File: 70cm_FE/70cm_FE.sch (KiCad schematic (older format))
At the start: 150 parts, among them J2 U.FL, J3 U.FL, J4 U.FL, Q1 2SC3356, Q2 2SC3356, Q3 2SC3356, Q4 2N7002, U1 HT7533-1, U2 74HC14, U3 74HC14, U4 LM393, U5 M68710L

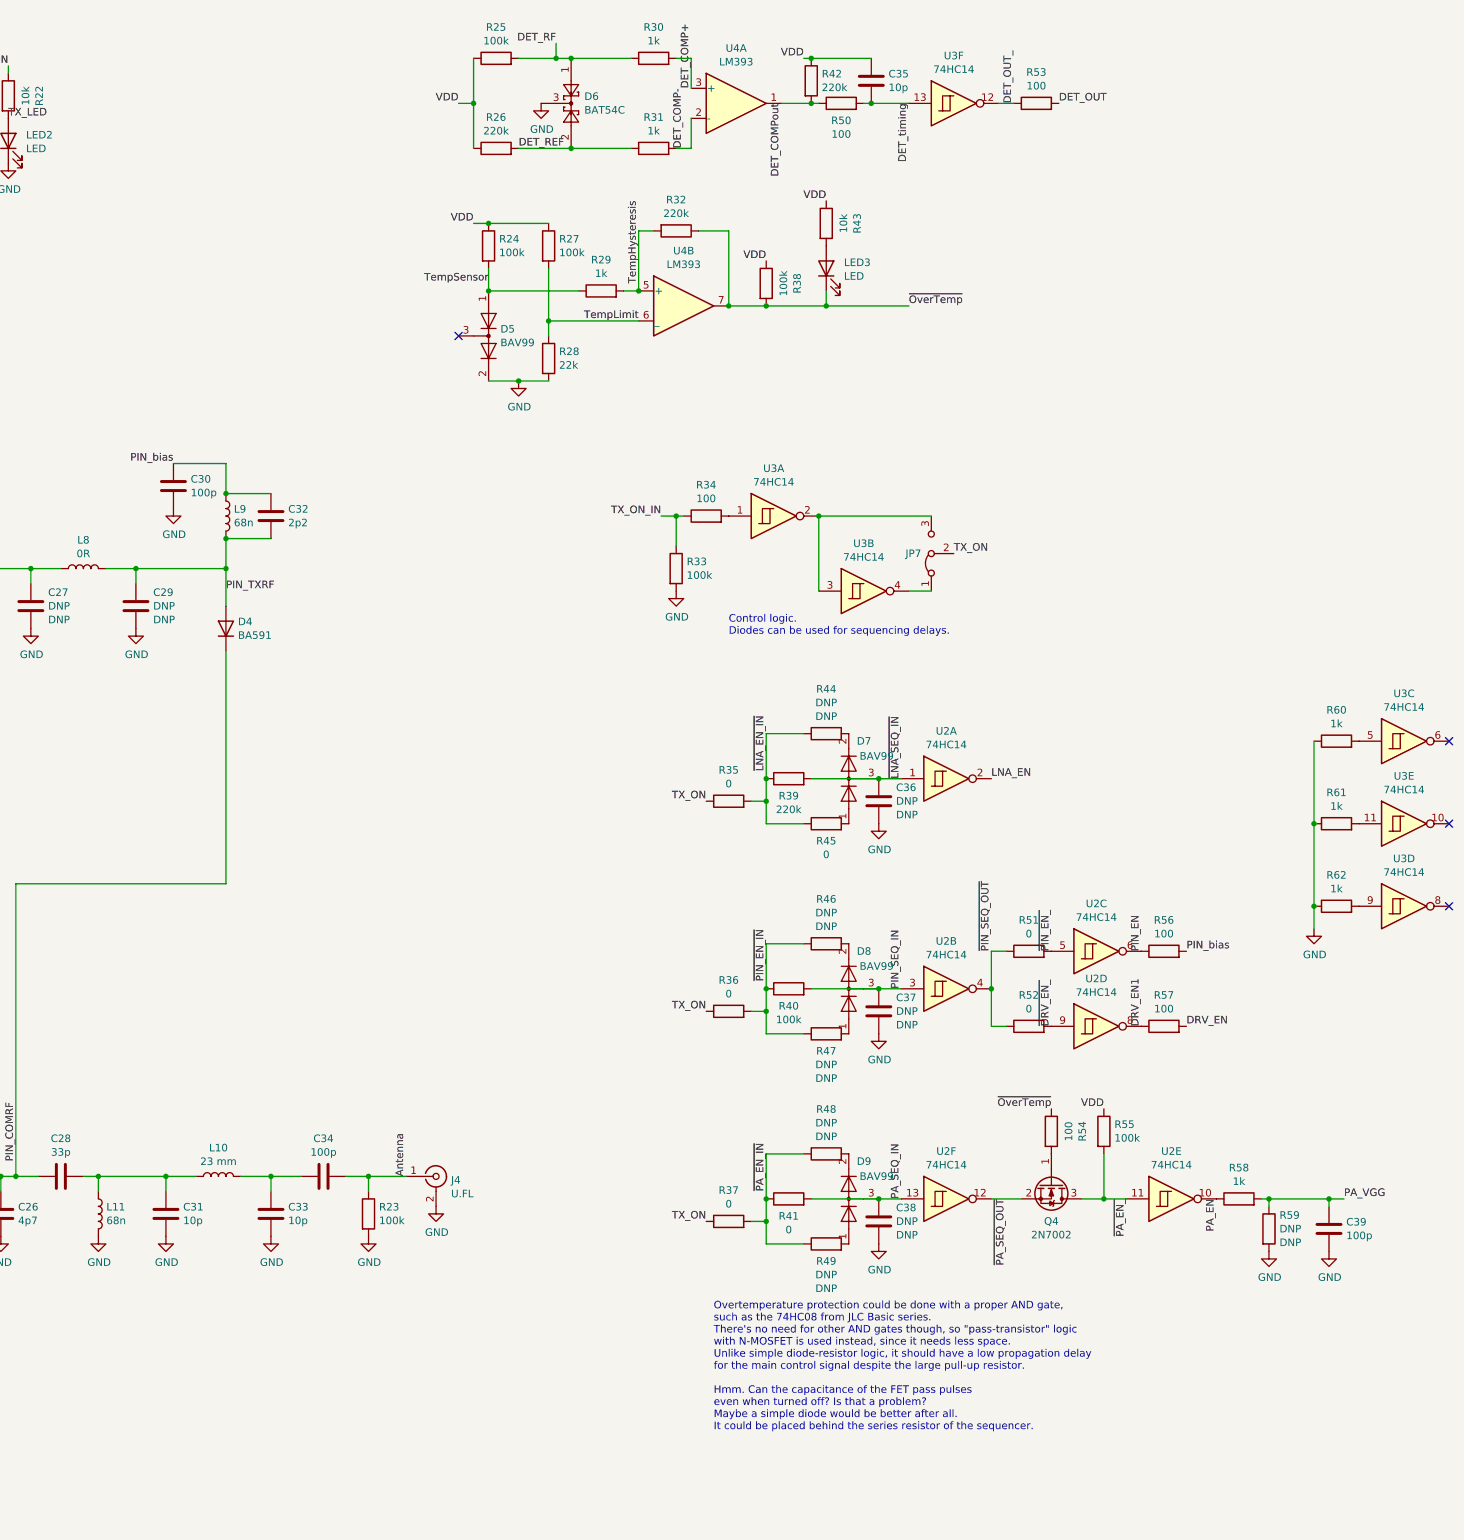
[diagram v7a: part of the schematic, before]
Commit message: Simplify and improve control circuits, do layout
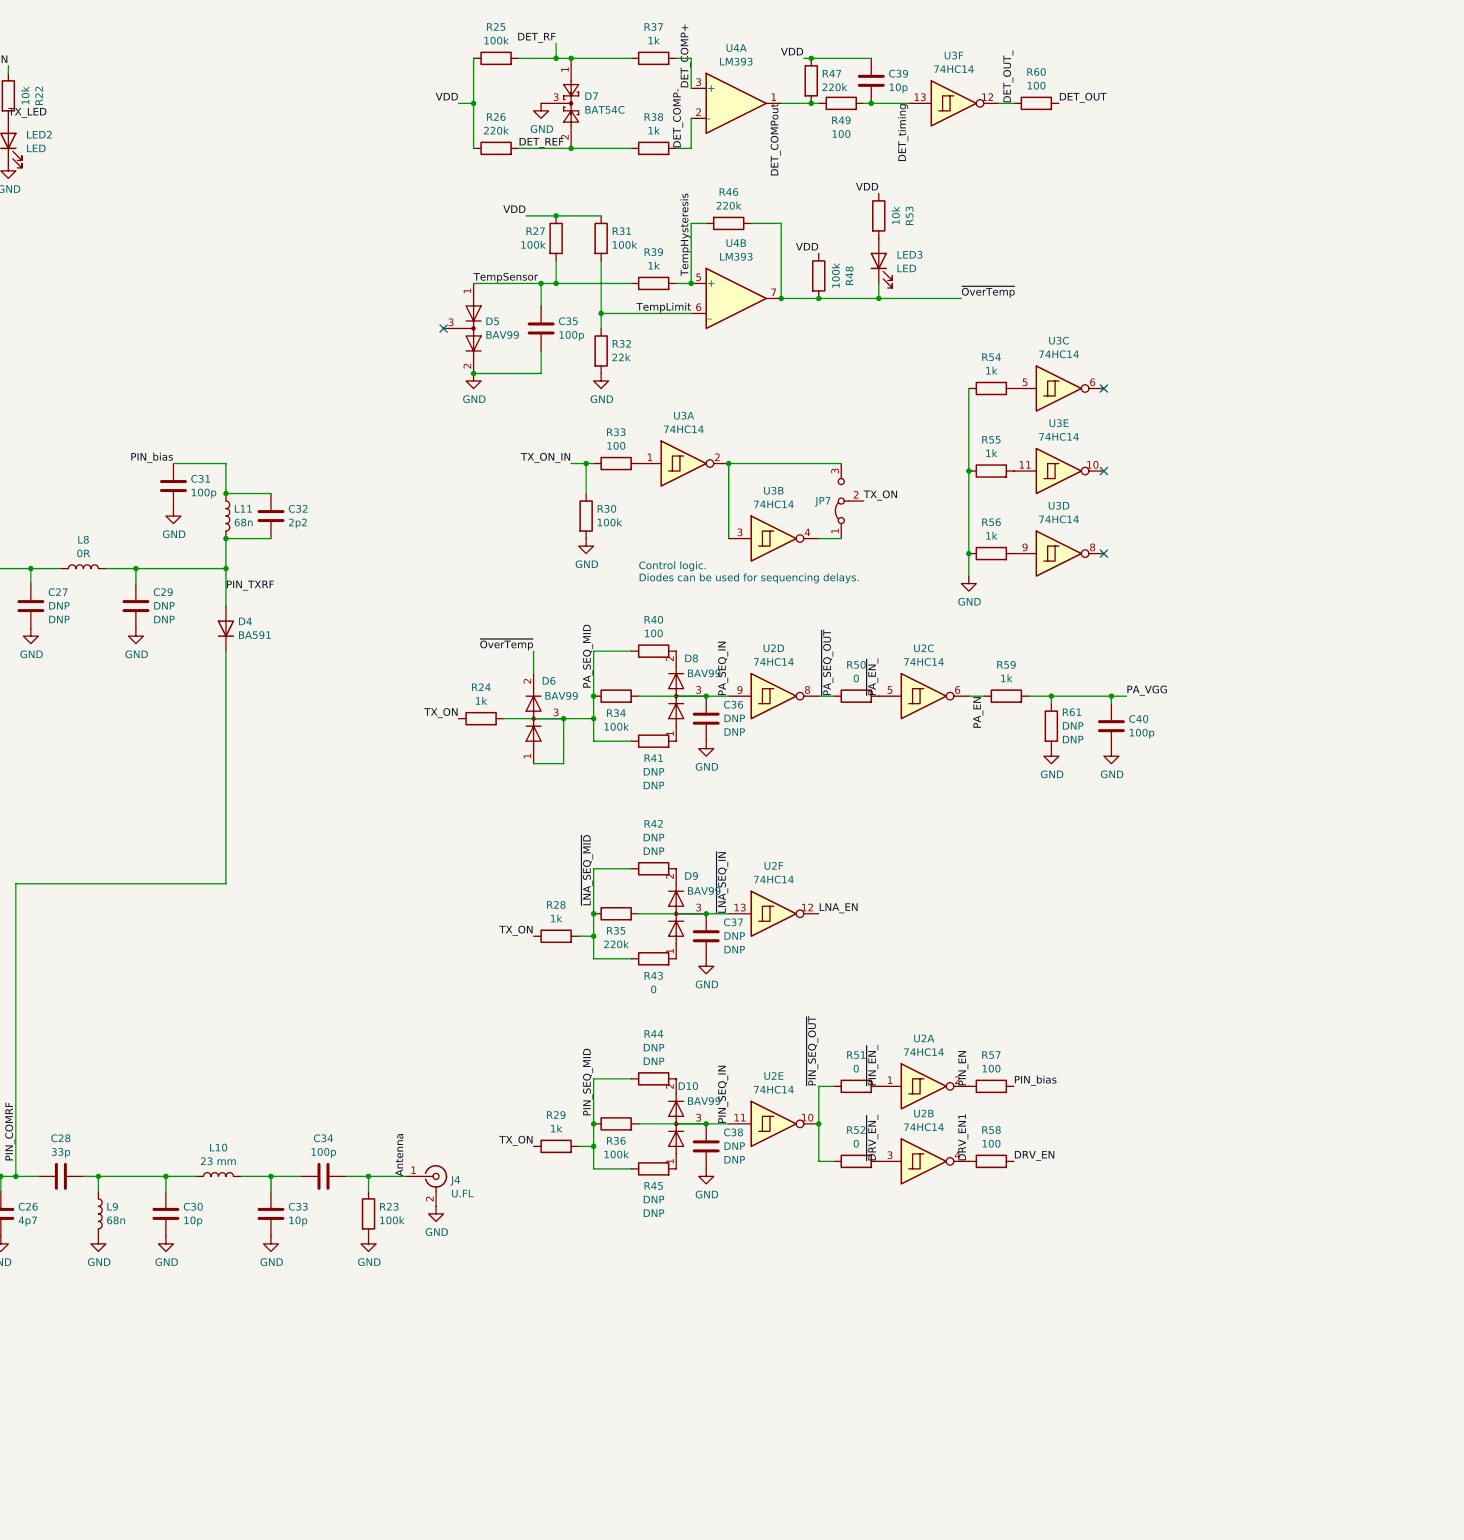
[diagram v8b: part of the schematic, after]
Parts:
- removed Q4: 2N7002, Package_TO_SOT_SMD:SOT-23, symbol Transistor_FET:2N7002
- removed R54: 100, Resistor_SMD:R_0402_1005Metric, symbol Device:R
- removed R55: 100k, Resistor_SMD:R_0402_1005Metric, symbol Device:R
- added C35: 100p, Capacitor_SMD:C_0603_1608Metric, symbol Device:C
- added D6: BAV99, Package_TO_SOT_SMD:SOT-23, symbol Diode:BAV99
- added R50: 0, Resistor_SMD:R_0402_1005Metric, symbol Device:R
- R24: renamed from R37; value 0 -> 1k
- R28: renamed from R35; value 0 -> 1k
- R29: renamed from R36; value 0 -> 1k
- R34: renamed from R41; value 0 -> 100k
- R40: renamed from R48; value DNP -> 100; DNP DNP -> (none)
- renumbered C31 to C30, C30 to C31, C38 to C36, C36 to C37, C37 to C38, C35 to C39, C39 to C40, D8 to D10, D6 to D7, D9 to D8, D7 to D9, L9 to L11, L11 to L9, R24 to R27, R33 to R30, R27 to R31, R28 to R32, R34 to R33, R39 to R35, R40 to R36, R30 to R37, R31 to R38, R29 to R39, R49 to R41, R44 to R42, R45 to R43, R46 to R44, R47 to R45, R32 to R46, R42 to R47, R38 to R48, R50 to R49, R43 to R53, R60 to R54, R61 to R55, R62 to R56, R56 to R57, R57 to R58, R58 to R59, R53 to R60, R59 to R61
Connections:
- net DRV_EN1: now also U2.4; no longer U2.8
- net GND: now also C35.2
- net LNA_EN: now also U2.12; no longer U2.2
- net PA_EN: now also U2.6; no longer U2.10
- net PA_SEQ_IN: now also U2.9; no longer U2.13
- net PIN_EN: now also U2.2; no longer U2.6
- net PIN_SEQ_IN: now also U2.11; no longer U2.3
- net TempSensor: now also C35.1
- net ~DRV_EN_~: now also U2.3; no longer U2.9
- net ~LNA_SEQ_IN~: now also U2.13; no longer U2.1
- net ~OverTemp~: now also D6.2 (A)
- net ~PA_EN_~: now also U2.5, R50.2; no longer U2.11
- net ~PA_SEQ_OUT~: now also U2.8, R50.1; no longer U2.12
- net ~PIN_EN_~: now also U2.1; no longer U2.5
- net ~PIN_SEQ_OUT~: now also U2.10; no longer U2.4
- net ~LNA_EN_IN~ renamed ~LNA_SEQ_MID~
- net ~PA_EN_IN~ renamed PA_SEQ_MID
- net PA_SEQ_MID: now also D6.1 (K), D6.3 (K)
- net ~PIN_EN_IN~ renamed PIN_SEQ_MID
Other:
- note removed: "Overtemperature protection could be done with a proper AND gate,\nsuch as the 74HC08 from JLC Basic series.\nThere's no need for other AND gates though, so "pass-transistor" logic\nwith N-MOSFET is used instead, since it needs less space.\nUnlike simple diode-resistor logic, it should have a low propagation delay\nfor the main control signal despite the large pull-up resistor.\n\nHmm. Can the cap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"
- moved on the sheet: C36, C37, C38, C40, D10, D5, D8, D9, JP7, LED3, R24, R27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
